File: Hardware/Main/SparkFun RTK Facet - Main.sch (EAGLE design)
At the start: 105 parts, among them J1 QWIIC_RIGHT_ANGLE, J10 FPC_12_0.5MM_BACKFLIP, J15 FPC_12_0.5MM_BACKFLIP, J18 FPC_12_0.5MM_BACKFLIP, J2 U.FL, J8 FPC_12_0.5MM_BACKFLIP, J9 CORTEX_JTAG_DEBUG_PTH, Q2 MBT3904DW1T1, Q3 SIL2308, U1 74HC4052D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

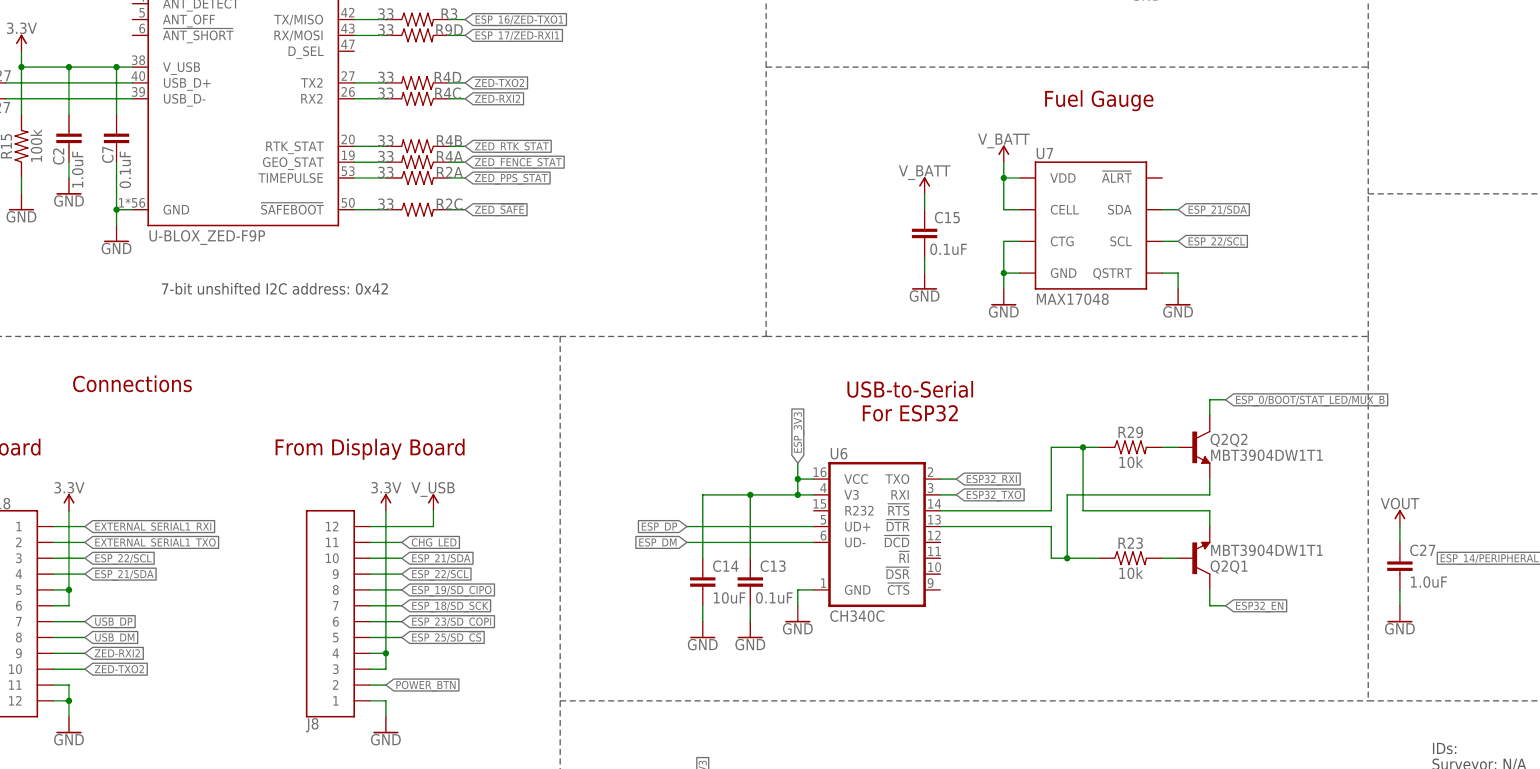
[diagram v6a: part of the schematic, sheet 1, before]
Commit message: Add I2C addresses to schematics
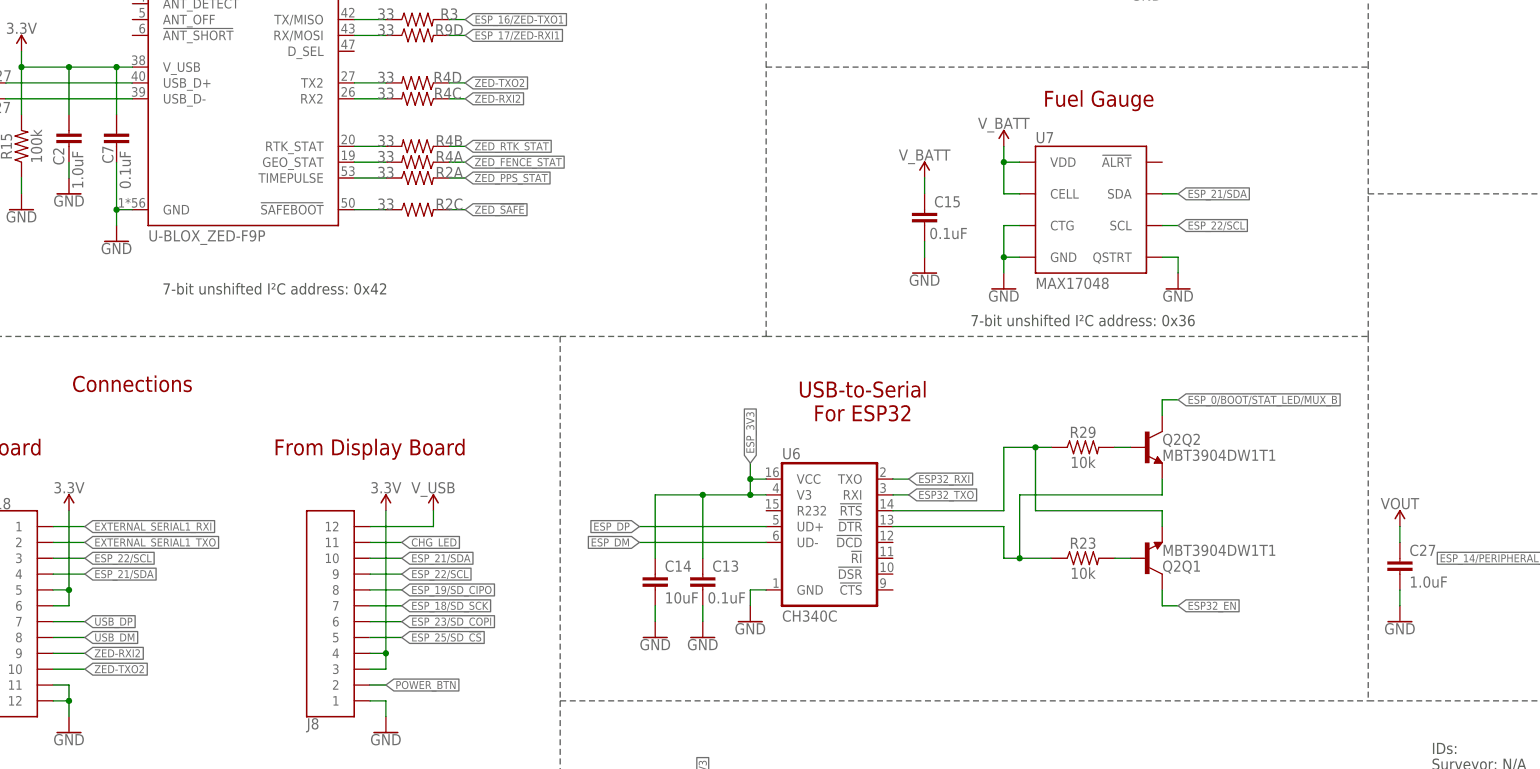
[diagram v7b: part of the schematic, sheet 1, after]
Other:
- note added: "7-bit unshifted I²C address: 0x2C"
- note added: "7-bit unshifted I²C address: 0x36"
- note added: "7-bit unshifted I²C address: 0x42"
- note removed: "7-bit unshifted I2C address: 0x2C"
- note removed: "7-bit unshifted I2C address: 0x42"
- moved on the sheet: C13, C14, C15, Q2Q1, Q2Q2, R23, R29, U6, U7

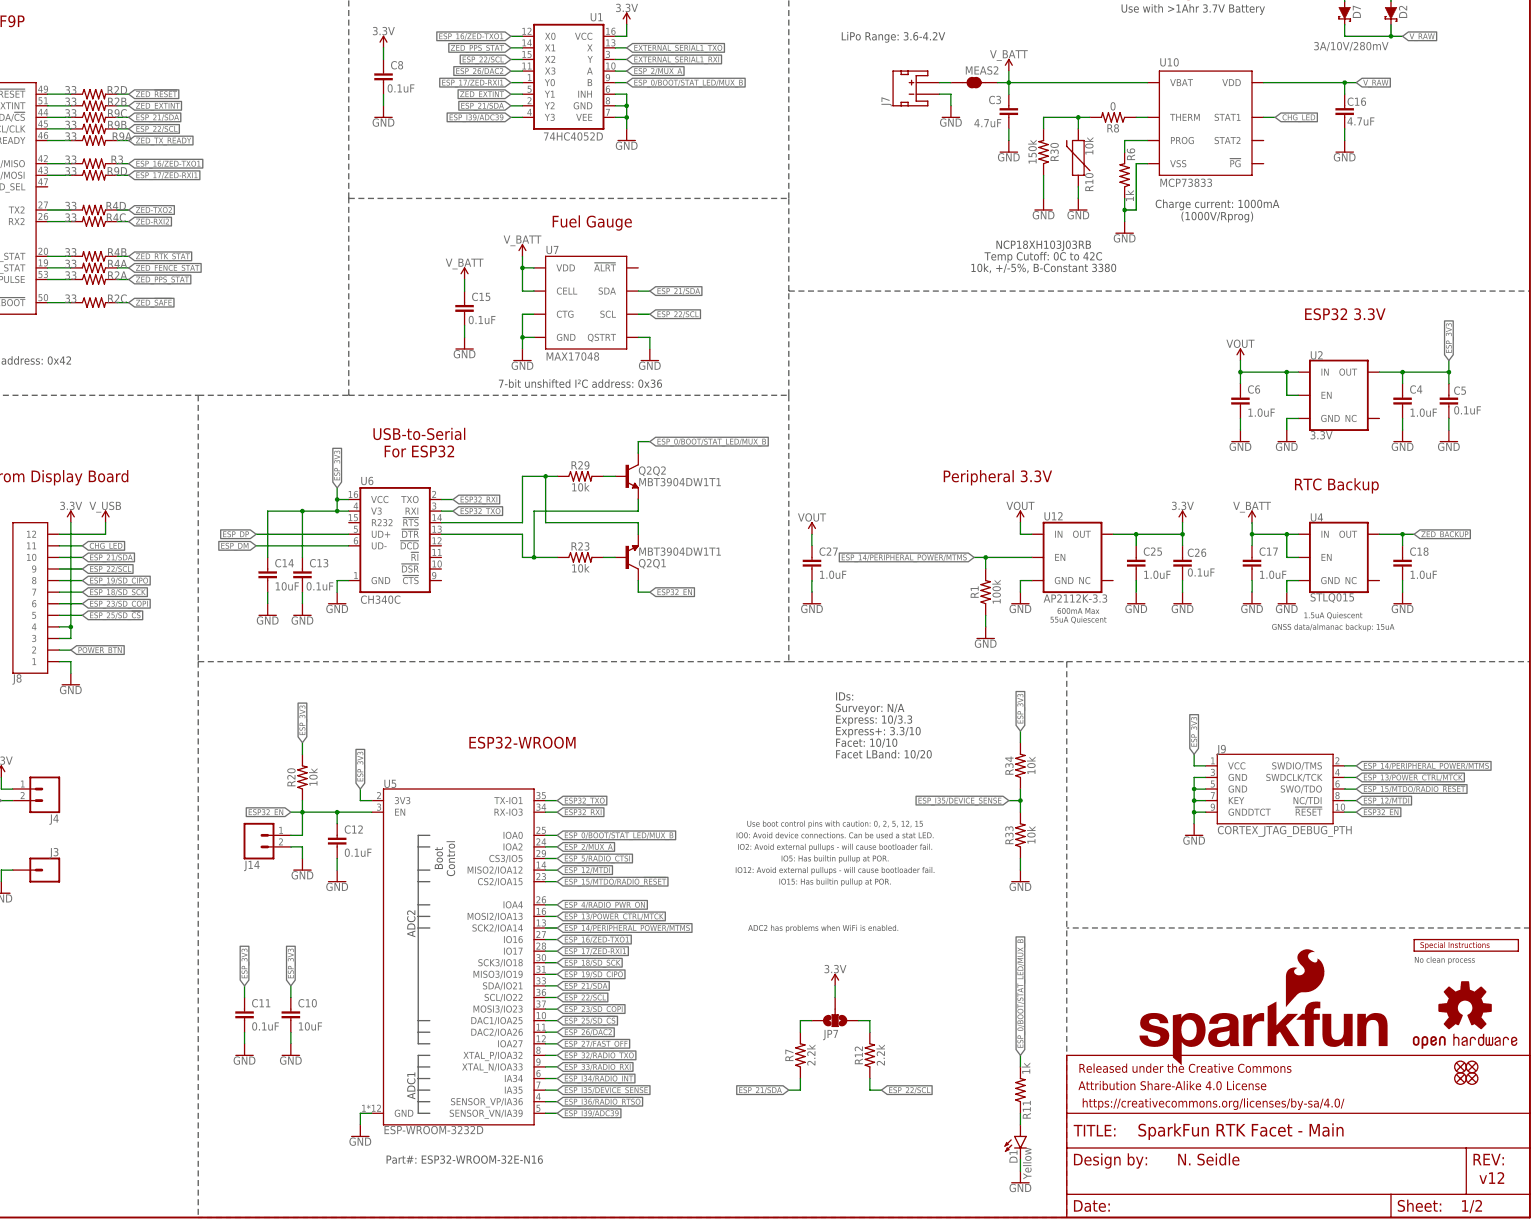
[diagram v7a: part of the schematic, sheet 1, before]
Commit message: Facet v13: change charger IC FP, discrete 33s, change cream on ESP32.
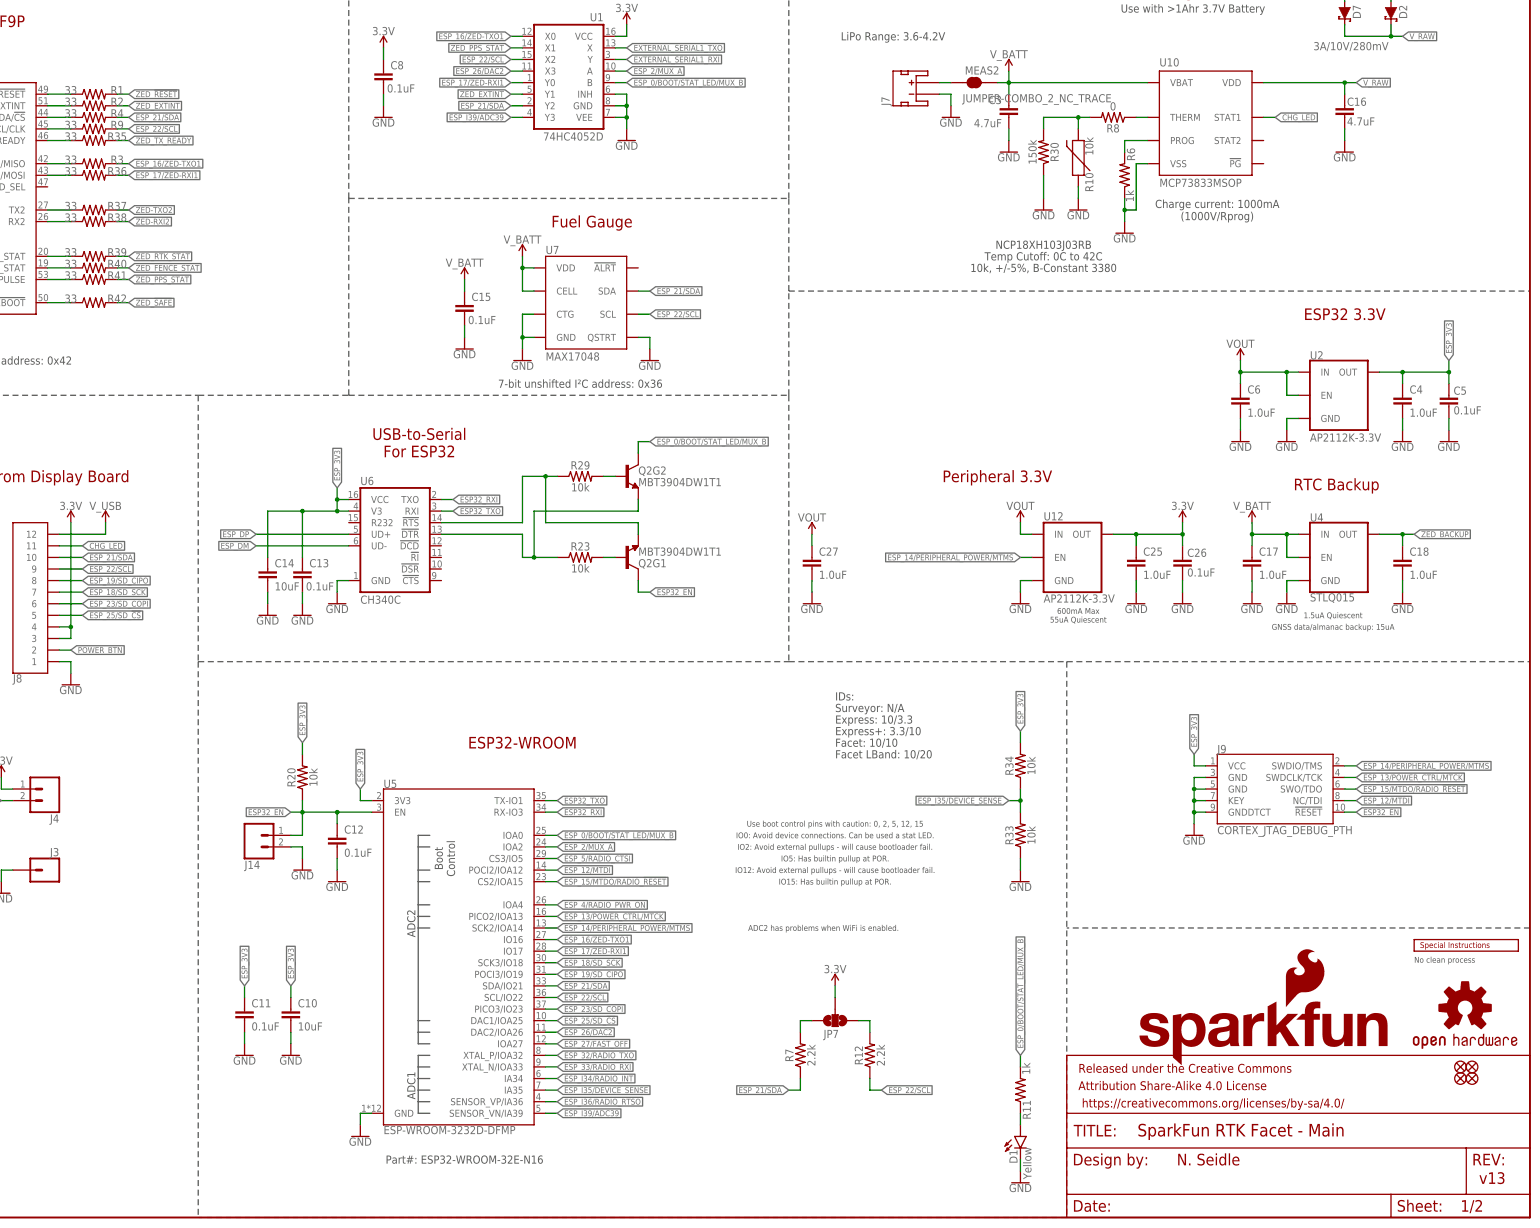
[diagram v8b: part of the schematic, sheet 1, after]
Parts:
- added R35, R36, R37, R38, R39, R40, R41, R42: 33, SparkFun-Resistors:33OHM-0603-1/10W-1%
- FB1: device SparkFun-Coils:FERRITE_BEAD-0402-2.66OHM-1GHZ -> SparkFun-Coils:FERRITE_BEAD-0402-2.66Ω-1GHZ
- R1: value 100k -> 33; device SparkFun-Resistors:100KOHM-0603-1/10W-1% -> SparkFun-Resistors:33OHM-0603-1/10W-1%
- R2, R4, R9: device SparkFun-Resistors:33OHM_RA-1206-1/16W-5% -> SparkFun-Resistors:33OHM-0603-1/10W-1%
- R25, R32: value 22 -> 22Ω
- U10: value MCP73833 -> MCP73833MSOP; device SparkFun-IC-Power:MCP73833 -> SparkFun-IC-Power:MCP73833MSOP
- U12: value AP2112K-3.3 -> AP2112K-3.3V
- U2: value 3.3V -> AP2112K-3.3V
- U5: value ESP-WROOM-3232D -> ESP-WROOM-3232D-DFMP; device SparkFun-RF:ESP-WROOM-3232D -> SparkFun-RF:ESP-WROOM-3232D-DFMP
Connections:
- net ESP32_!DTR: now also Q2G2.E; no longer Q2Q2.E
- net ESP32_!RTS: now also Q2G1.E; no longer Q2Q1.E
- net ESP32_EN: now also Q2G1.C; no longer Q2Q1.C
- net ESP_0/BOOT/STAT_LED/MUX_B: now also Q2G2.C; no longer Q2Q2.C
- net ESP_12/MTDI: now also U5.POCI2/IOA12; no longer U5.MISO2/IOA12
- net ESP_13/POWER_CTRL/MTCK: now also U5.PICO2/IOA13; no longer U5.MOSI2/IOA13
- net ESP_14/PERIPHERAL_POWER/MTMS: no longer R1.2
- net ESP_17/ZED-RXI1: now also R36.2; no longer R9D.2
- net ESP_19/SD_CIPO: now also U5.POCI3/IO19; no longer U5.MISO3/IO19
- net ESP_21/SDA: now also R4.2; no longer R9C.2
- net ESP_22/SCL: now also R9.2; no longer R9B.2
- net ESP_23/SD_COPI: now also U5.PICO3/IO23; no longer U5.MOSI3/IO23
- net FENCE_LV: now also R40.1; no longer R4A.2
- net GND: no longer R1.1
- net N$16: now also R1.1; no longer R2D.1
- net N$18: now also R42.1; no longer R2C.1
- net N$22: now also R35.1; no longer R9A.1
- net N$24: now also Q2G1.B; no longer Q2Q1.B
- net N$25: now also Q2G2.B; no longer Q2Q2.B
- net N$5: now also R2.1; no longer R2B.1
- net PPS: now also R41.1; no longer R2A.1
- net RTK_LV: now also R39.1; no longer R4B.2
- net RX2_LV: now also R38.1; no longer R4C.2
- net RXLV: now also R36.1; no longer R9D.1
- net SCL_LV: now also R9.1; no longer R9B.1
- net SDA_LV: now also R4.1; no longer R9C.1
- net TX2_LV: now also R37.1; no longer R4D.2
- net ZED-RXI2: now also R38.2; no longer R4C.1
- net ZED-TXO2: now also R37.2; no longer R4D.1
- net ZED_!RESET!: now also R1.2; no longer R2D.2
- net ZED_!SAFE!: now also R42.2; no longer R2C.2
- net ZED_EXTINT: now also R2.2; no longer R2B.2
- net ZED_FENCE_STAT: now also R40.2; no longer R4A.1
- net ZED_PPS_STAT: now also R41.2; no longer R2A.2
- net ZED_RTK_STAT: now also R39.2; no longer R4B.1
- net ZED_TX_READY: now also R35.2; no longer R9A.2
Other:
- note added: "v13"
- note removed: "v12"
- moved on the sheet: R1
